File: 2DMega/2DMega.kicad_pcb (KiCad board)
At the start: 2 copper layers, 114.3 x 114.3 mm, 43 parts, among them J1 Conn_01x06_Male, J2 Conn_01x06_Female, J3 Conn_02x03_Odd_Even, J4 Conn_01x06_Male, J5 Conn_01x06_Female, P1 Power, P10 CONN_01X01, P11 CONN_01X01, P12 CONN_01X01, P13 CONN_01X01, P2 Analog, P3 Analog, P4 Digital, P5 PWM, P6 PWM, P7 Communication, P8 CONN_01X01, P9 CONN_01X01, SW1 SW_SPST, U1 HDSP-A153

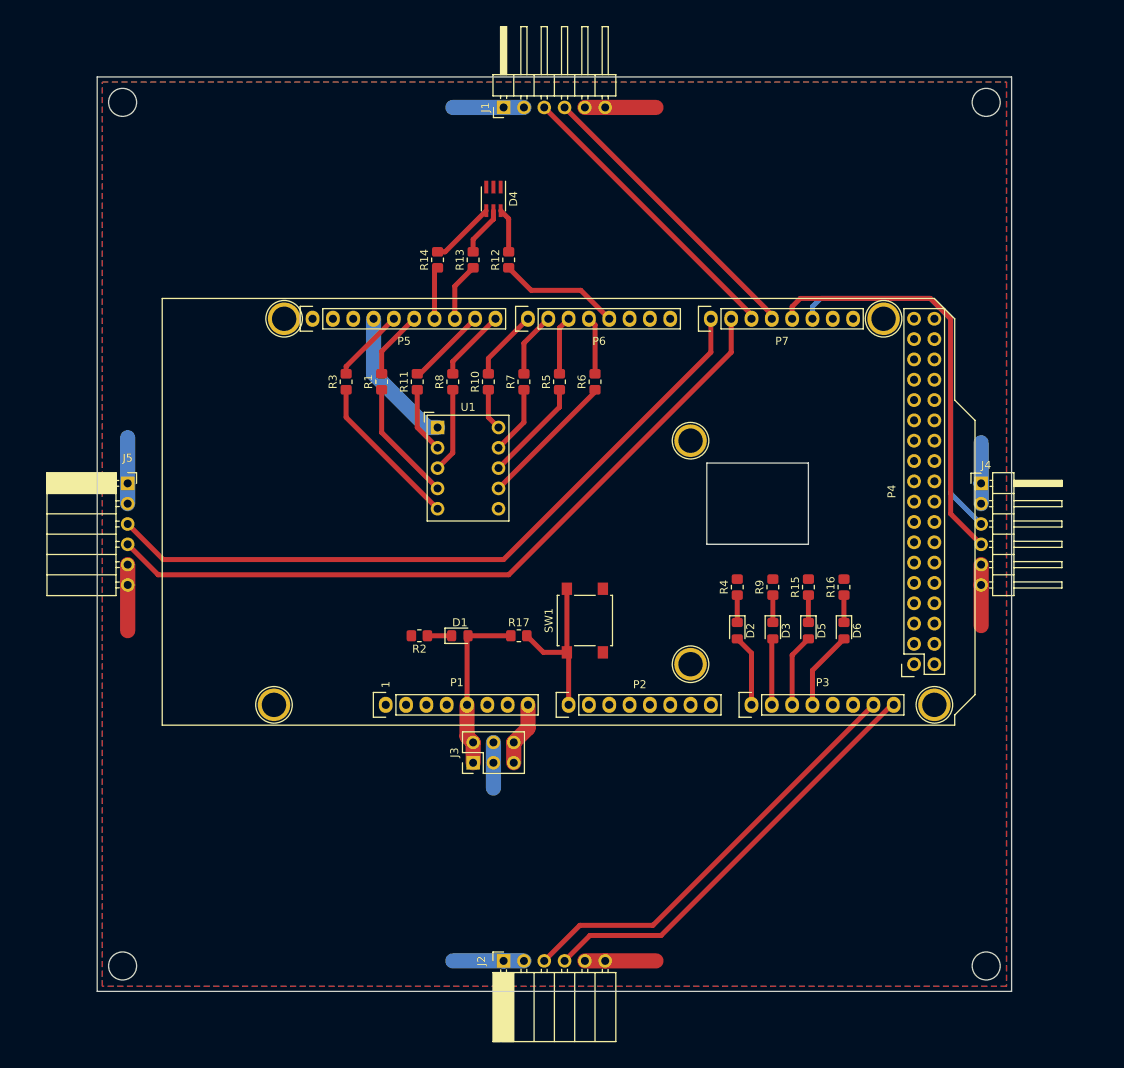
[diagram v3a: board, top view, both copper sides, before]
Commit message: Added resistors to tx and rx pins, silkscreen tags
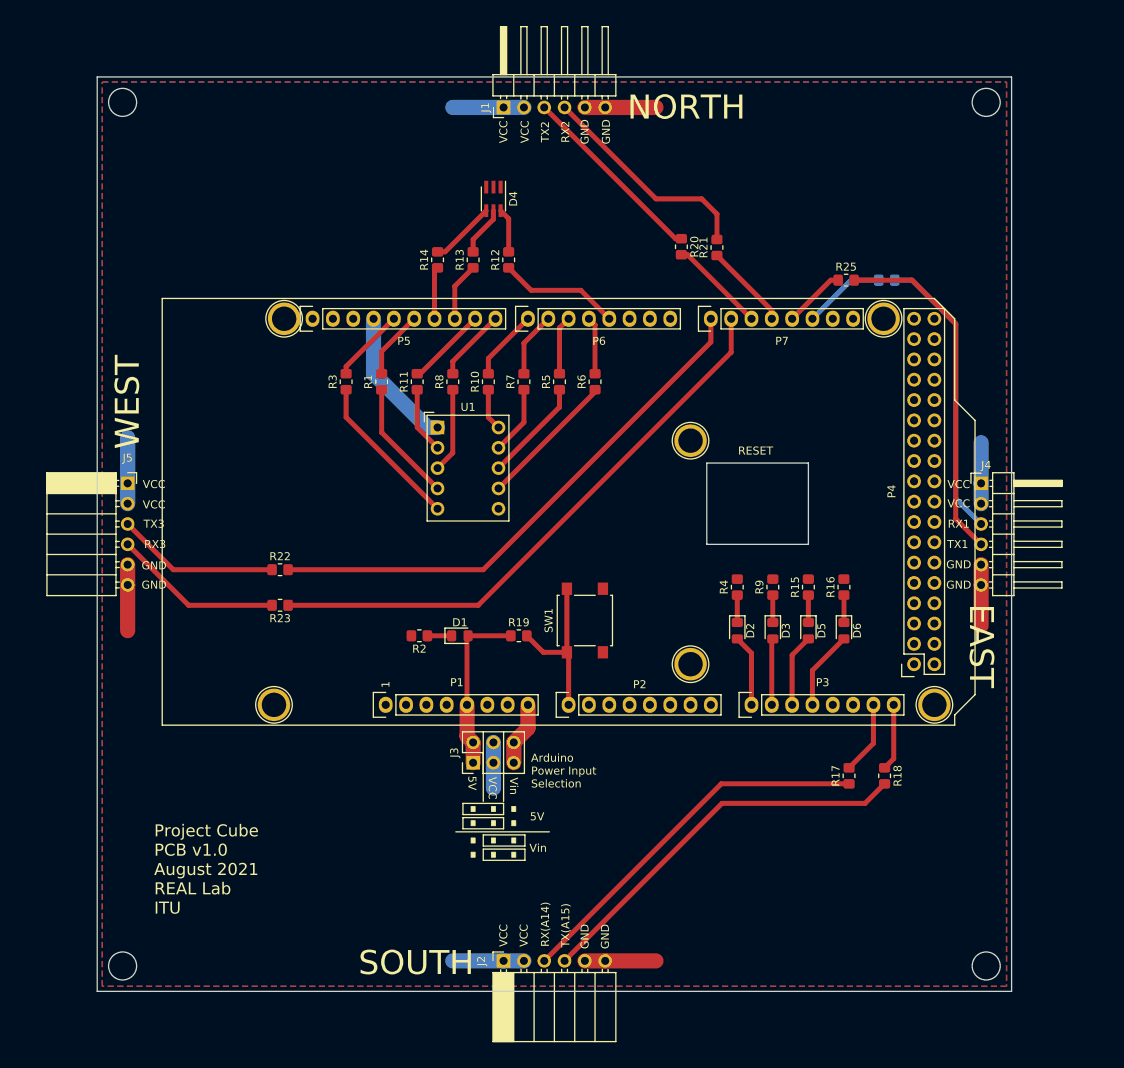
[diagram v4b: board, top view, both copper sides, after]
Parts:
- added R17: 330, Resistor_SMD:R_0805_2012Metric_Pad1.20x1.40mm_HandSolder, F.Cu at (189.2, 128.0)
- added R18: 330, Resistor_SMD:R_0805_2012Metric_Pad1.20x1.40mm_HandSolder, F.Cu at (193.7, 128.0)
- added R20: 330, Resistor_SMD:R_0805_2012Metric_Pad1.20x1.40mm_HandSolder, F.Cu at (168.3, 61.9)
- added R21: 330, Resistor_SMD:R_0805_2012Metric_Pad1.20x1.40mm_HandSolder, F.Cu at (172.7, 62.0)
- added R22: 330, Resistor_SMD:R_0805_2012Metric_Pad1.20x1.40mm_HandSolder, F.Cu at (118.1, 102.2)
- added R23: 330, Resistor_SMD:R_0805_2012Metric_Pad1.20x1.40mm_HandSolder, F.Cu at (118.1, 106.7)
- added R24: 330, Resistor_SMD:R_0805_2012Metric_Pad1.20x1.40mm_HandSolder, B.Cu at (193.9, 66.0)
- added R25: 330, Resistor_SMD:R_0805_2012Metric_Pad1.20x1.40mm_HandSolder, F.Cu at (188.9, 66.0)
- renumbered R17 to R19
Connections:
- J1 pad 3: /16(Tx2) -> Net-(J1-Pad3)
- J1 pad 4: /17(Rx2) -> Net-(J1-Pad4)
- J2 pad 3: /A14 -> Net-(J2-Pad3)
- J2 pad 4: /A15 -> Net-(J2-Pad4)
- J4 pad 3: /19(Rx1) -> Net-(J4-Pad3)
- J4 pad 4: /18(Tx1) -> Net-(J4-Pad4)
- J5 pad 3: /14(Tx3) -> Net-(J5-Pad3)
- J5 pad 4: /15(Rx3) -> Net-(J5-Pad4)
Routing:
- net Net-(J2-Pad4): track 0.00 -> 49.2 mm
- net Net-(J2-Pad3): track 0.00 -> 47.3 mm
- net /A15: track 54.4 -> 8.35 mm
- net /A14: track 54.9 -> 9.64 mm
- net /18(Tx1): track 52.6 -> 7.75 mm
- net Net-(J4-Pad4): track 0.00 -> 43.8 mm
- net /19(Rx1): track 47.5 -> 10.3 mm
- net Net-(J4-Pad3): track 0.00 -> 36.2 mm
- net Net-(J1-Pad4): track 0.00 -> 27.7 mm
- net /17(Rx2): track 37.5 -> 11.1 mm
- net /16(Tx2): track 37.4 -> 12.3 mm
- net Net-(J1-Pad3): track 0.00 -> 23.9 mm
- net /14(Tx3): track 90.0 -> 67.9 mm
- net Net-(J5-Pad4): track 0.00 -> 21.2 mm
- net Net-(J5-Pad3): track 0.00 -> 20.4 mm
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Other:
- board text added: "5V"
- board text added: "Arduino Power Input Selection"
- board text added: "EAST"
- board text added: "GND"
- board text added: "NORTH"
- board text added: "Project Cube PCB v1.0 August 2021 REAL Lab ITU"
- board text added: "RESET"
- board text added: "RX(A14)"
- board text added: "RX1"
- board text added: "RX2"
- board text added: "RX3"
- board text added: "SOUTH"
- board text added: "TX(A15)"
- board text added: "TX1"
- board text added: "TX2"
- board text added: "TX3"
- board text added: "VCC"
- board text added: "Vin"
- board text added: "WEST"

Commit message: As built
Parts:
- R1, R10, R11, R3, R5, R6, R7, R8: value 200 -> 300
